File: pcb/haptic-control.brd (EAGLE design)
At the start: 40 x 160 mm, 117 parts, among them M1 SPH0641LM4H-1, P1 2P-PAD_1X3.5, P2 2P-PAD_1X3.5, P3 2P-PAD_1X3.5, P4 2P-PAD_1X3.5, U1 CC2642R, U10 FS8205, U11 MIC23159, U12 DRV2605L, U2 SST26VF064B, U3 ICM20948, U4 74LVC1G17, U5 DRV2605L, U6 PCA9306-DCU, U7 MTCH6301, U8 BQ51050B, U9 FS312F-G, X1 48MHz, X2 32.768kHz

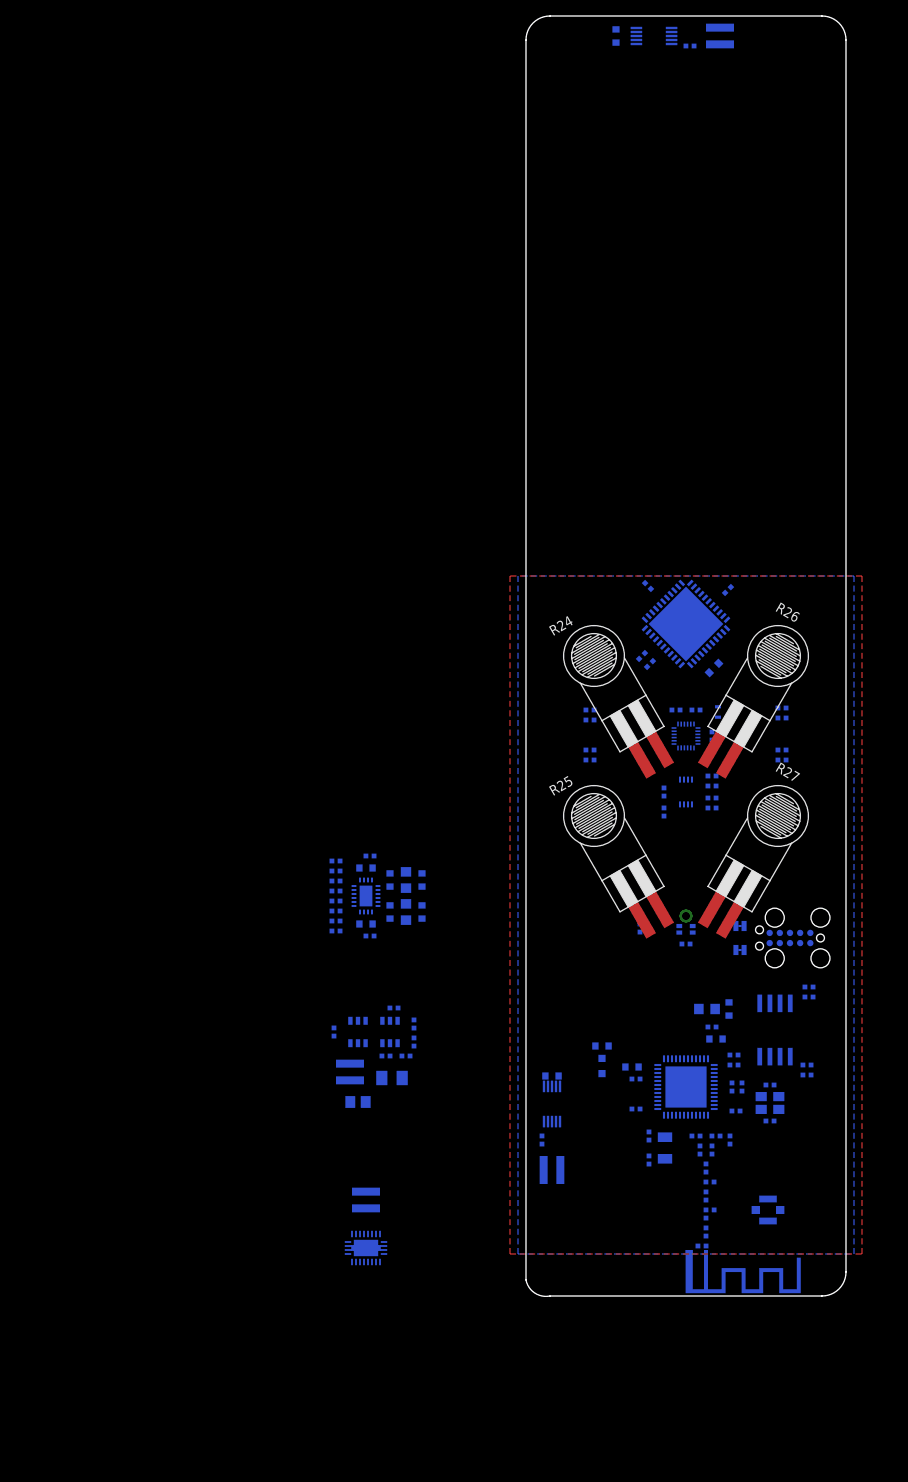
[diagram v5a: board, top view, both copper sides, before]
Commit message: Add QI and conect MCU
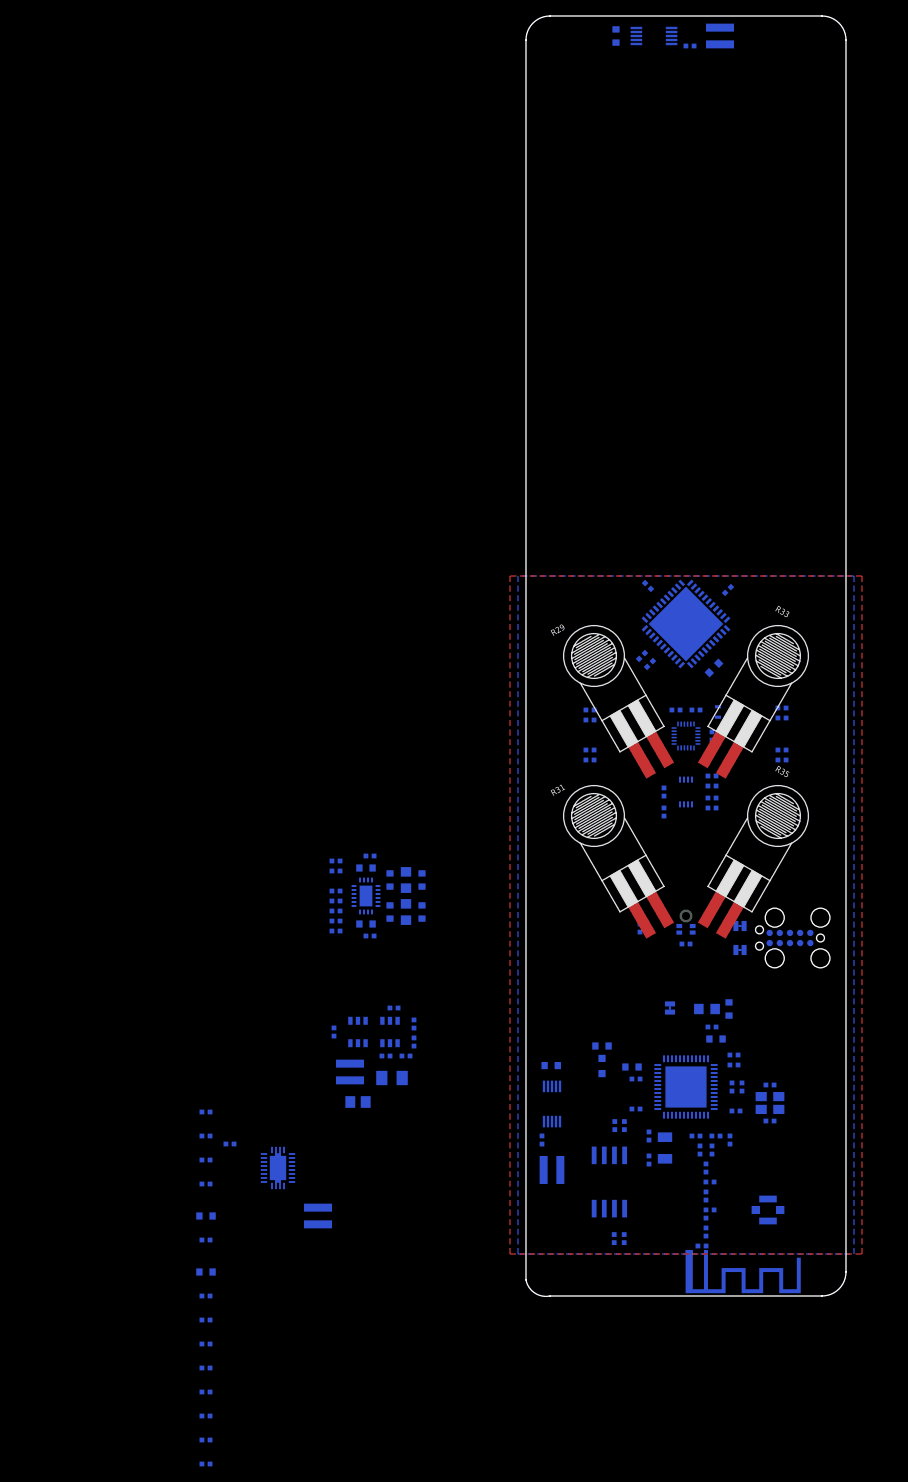
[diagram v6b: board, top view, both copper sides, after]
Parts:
- removed R1: 100k, Passive Components > Resistors > Chip Resistors:_0402
- added C52, C55, C56: 470p, Passive Components > Capacitors > Multilayer Ceramic Capacitors MLCC:_0402
- added C53, C57, C58, C59, C61: 100n, Passive Components > Capacitors > Multilayer Ceramic Capacitors MLCC:_0402
- added C54: 1u, Passive Components > Capacitors > Multilayer Ceramic Capacitors MLCC:0603_WAVE
- added C60: 10u, Passive Components > Capacitors > Multilayer Ceramic Capacitors MLCC:0603_WAVE
- added JP3: JUMPER-SMT_2_NC_TRACE_SILK, Utility > Board:SMT-JUMPER_2_NC_TRACE_SILK
- added R32, R34, R36: 3.4k, Passive Components > Resistors > Chip Resistors:_0402
- added R33, R35: FSR400-SHORT-TAIL, Interlink:FSR400-SHORT-TAIL
- added R37: 100k, Passive Components > Resistors > Chip Resistors:_0402
- C1: value 100n -> 1u; device Passive Components > Capacitors > Multilayer Ceramic Capacitors MLCC:_0402 -> Passive Components > Capacitors > Multilayer Ceramic Capacitors MLCC:0603_WAVE
- C10, C9: value 12p -> 22n
- C11, C12: value DNP -> 470n
- C13: value 1u -> 470p; device Passive Components > Capacitors > Multilayer Ceramic Capacitors MLCC:0603_WAVE -> Passive Components > Capacitors > Multilayer Ceramic Capacitors MLCC:_0402
- C14, C15, C19, C2: value 100n -> 4u7; device Passive Components > Capacitors > Multilayer Ceramic Capacitors MLCC:_0402 -> Passive Components > Capacitors > Multilayer Ceramic Capacitors MLCC:0603_WAVE
- C16, C39: value 4u7 -> 1u
- C18: value 100n -> 470p
- C21: value 100n -> 100u; device Passive Components > Capacitors > Multilayer Ceramic Capacitors MLCC:_0402 -> Passive Components > Capacitors > Multilayer Ceramic Capacitors MLCC:_1206
- C22, C44: value 100n -> DNP
- C23, C36: value 100n -> 22u; device Passive Components > Capacitors > Multilayer Ceramic Capacitors MLCC:_0402 -> Passive Components > Capacitors > Multilayer Ceramic Capacitors MLCC:0603_WAVE
- C24: value 10u -> 1p8; device Passive Components > Capacitors > Multilayer Ceramic Capacitors MLCC:0603_WAVE -> Passive Components > Capacitors > Multilayer Ceramic Capacitors MLCC:_0402
- C26: value 100n -> 12p; device Passive Components > Capacitors > Multilayer Ceramic Capacitors MLCC:_0402 -> Passive Components > Capacitors > Multilayer Ceramic Capacitors MLCC:_0402_SEL
- C27: value 22u -> 100n; device Passive Components > Capacitors > Multilayer Ceramic Capacitors MLCC:0603_WAVE -> Passive Components > Capacitors > Multilayer Ceramic Capacitors MLCC:_0402
- C28, C29: value 1p -> 100n
- C30: value 12p -> 1p
- C31: value 1p -> 22u; device Passive Components > Capacitors > Multilayer Ceramic Capacitors MLCC:_0402 -> Passive Components > Capacitors > Multilayer Ceramic Capacitors MLCC:0603_WAVE
- C32: value 1p8 -> 100n
- C33: value 12p -> 1p; device Passive Components > Capacitors > Multilayer Ceramic Capacitors MLCC:_0402_SEL -> Passive Components > Capacitors > Multilayer Ceramic Capacitors MLCC:_0402
- C34: value 470p -> 1p
- C35: value DNP -> 12p
- C37, C38, C46, C47: value 1u -> 100n; device Passive Components > Capacitors > Multilayer Ceramic Capacitors MLCC:0603_WAVE -> Passive Components > Capacitors > Multilayer Ceramic Capacitors MLCC:_0402
- C4: value 22u -> 4u7
- C40, C48, C49: value 470p -> 100n
- C41: value 470p -> DNP
- C42: value 4u7 -> 12p; device Passive Components > Capacitors > Multilayer Ceramic Capacitors MLCC:0603_WAVE -> Passive Components > Capacitors > Multilayer Ceramic Capacitors MLCC:_0402
- C43: value 100u -> 12p; device Passive Components > Capacitors > Multilayer Ceramic Capacitors MLCC:_1206 -> Passive Components > Capacitors > Multilayer Ceramic Capacitors MLCC:_0402
- C5: value 100n -> 1n
- C50: value 470p -> 1u; device Passive Components > Capacitors > Multilayer Ceramic Capacitors MLCC:_0402 -> Passive Components > Capacitors > Multilayer Ceramic Capacitors MLCC:0603_WAVE
- C6: value 22u -> 470p; device Passive Components > Capacitors > Multilayer Ceramic Capacitors MLCC:0603_WAVE -> Passive Components > Capacitors > Multilayer Ceramic Capacitors MLCC:_0402
- C7, C8: value 100n -> 10n
- L1: value 6u8 -> 1u
- L2: value BLM18HE152SN1 -> 1u; device Passive Components > Inductors, Chokes & Coils:_0603 -> Passive Components > Inductors, Chokes & Coils:_0805
- L3: value 2n4 -> BLM18HE152SN1; device Passive Components > Inductors, Chokes & Coils:_0402 -> Passive Components > Inductors, Chokes & Coils:_0603
- L4: value 2n4 -> 2N
- L6: value 2N -> 2n4
- L7: value 1u -> 2n4; device Passive Components > Inductors, Chokes & Coils:_0805 -> Passive Components > Inductors, Chokes & Coils:_0402
- L8: value 1u -> 6u8
- R11: value 10M -> 1k2
- R12: value 100 -> 140
- R14: value 49.9k -> 10k
- R15: value 1k -> 100k
- R16: value 100k -> 49.9k
- R17: value 100k -> 100
- R18: value 309k -> 1k
- R19: value 71.5k -> 10M
- R2: value 100k -> 309k
- R22: value 301k -> 4k7
- R23: value 158k -> 4k7
- R24, R25: value FSR400-SHORT-TAIL -> 100k; device Interlink:FSR400-SHORT-TAIL -> Passive Components > Resistors > Chip Resistors:_0402
- R26, R27: value FSR400-SHORT-TAIL -> 4k7; device Interlink:FSR400-SHORT-TAIL -> Passive Components > Resistors > Chip Resistors:_0402
- R28: value 3.4k -> 200k
- R29, R31: value 3.4k -> FSR400-SHORT-TAIL; device Passive Components > Resistors > Chip Resistors:_0402 -> Interlink:FSR400-SHORT-TAIL
- R3: value 4k7 -> 71.5k
- R6: value 4k7 -> 100k
- R7: value 200k -> 301k
- R8: value 4k7 -> 158k
- R9: value 4k7 -> 2k43
- U1: value CC2642R -> MIC23159; device Texas Instruments:QFN48 -> Microchip:VQFN20
- U10: value FS8205 -> DRV2605L; device Fortune:SOT23-6 -> Texas Instruments:VSSOP10
- U11: value MIC23159 -> DRV2605L; device Microchip:VQFN20 -> Texas Instruments:VSSOP10
- U12: value DRV2605L -> MTCH6301; device Texas Instruments:VSSOP10 -> Microchip:QFN44
- U2: value SST26VF064B -> BQ51050B; device Microchip:WSOIC8 -> Texas Instruments:VQFN20
- U3: value ICM20948 -> FS312F-G; device TDK:QFN20 -> Fortune:SOT23-6
- U4: value 74LVC1G17 -> FS8205; device Semiconductors > Integrated Circuits - ICs > Logic ICs > Logic Gates:SC70-5 -> Fortune:SOT23-6
- U5: value DRV2605L -> CC2642R; device Texas Instruments:VSSOP10 -> Texas Instruments:QFN48
- U6: value PCA9306-DCU -> SST26VF064B; device Texas Instruments:VSSOP8 -> Microchip:WSOIC8
- U7: value MTCH6301 -> 74LVC1G17; device Microchip:QFN44 -> Semiconductors > Integrated Circuits - ICs > Logic ICs > Logic Gates:SC70-5
- U8: value BQ51050B -> ICM20948; device Texas Instruments:VQFN20 -> TDK:QFN20
- U9: value FS312F-G -> PCA9306-DCU; device Fortune:SOT23-6 -> Texas Instruments:VSSOP8
- moved U11 113.4 mm to (16.0, 157.5), turned to 180 degrees
- moved C47 88.3 mm to (23.2, 70.0), turned to 270 degrees
- moved C19 86.3 mm to (-40.0, 10.0)
- moved C12 83.3 mm to (-40.0, -18.0)
- moved C45 83.0 mm to (21.2, 73.2)
- moved C11 82.5 mm to (-40.0, -21.0), turned to 0 degrees
- moved R9 81.2 mm to (-40.0, 14.0), turned to 0 degrees
- moved R10 79.8 mm to (-37.0, 19.0), turned to 0 degrees
- moved C26 78.0 mm to (22.5, 10.2), turned to 270 degrees
- moved U8 75.5 mm to (20.0, 70.0), turned to 180 degrees
- moved C7 74.3 mm to (-40.0, -6.00), turned to 0 degrees
- moved C8 73.6 mm to (-40.0, -9.00), turned to 0 degrees
- moved U12 73.6 mm to (20.0, 84.0), turned to 45 degrees
- moved C5 73.1 mm to (-40.0, -3.00), turned to 0 degrees
- moved R24 72.9 mm to (11.0, 7.17), flipped to the bottom, turned to 270 degrees
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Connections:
- removed net 3V3_PG: R17.1, U11.15
- new net !QI_CHG: R10.1, U2.7, U5.18
- new net N$39: R11.2, R12.2, R13.1, U2.14
- new net N$40: R11.1, U2.12
- new net N$41: C17.P$1, R13.2, U2.18
- new net N$42: R9.2, U2.10
- new net N$43: C11.1, U2.5
- new net N$44: C9.1, U2.6
- new net N$45: C7.1, U2.3
- new net N$46: C12.1, U2.16
- new net N$47: C10.1, U2.15
- new net N$48: C8.1, U2.17
- new net N$49: C10.2, C12.2, C5.2, C8.2, P1.2, U2.19
- new net N$50: C11.2, C3.1, C5.1, C7.2, C9.2, U2.2
- new net N$51: C3.2, P1.1
- new net N$53: JP3.2, U1.15
- new net QI_CTRL: R14.2, U2.13, U5.19
- net 1.8V: now also C14.P$1, C46.1, C47.1, L2.1, R26.2, R27.2, R7.1, U1.10, U8.13, U8.8, U9.2; no longer C18.1, C19.1, C42.P$1, L8.1, R22.1, R8.2, R9.2, U11.10, U3.13, U3.8, U6.2
- net 1V8_PG: now also R6.1, U1.12, U5.20; no longer R21.1, U11.12
- net 3.3V: now also C23.P$1, C4.P$1, C40.1, C57.1, C58.1, C59.1, C61.1, L1.1, L3.1, R22.2, R23.2, R24.2, R25.2, R28.2, R29.1, R31.1, R33.1, R35.1, R37.2, U1.17, U12.17, U12.28, U12.40, U6.8, U7.3; no longer C15.1, C22.1, C23.1, C25.1, C26.1, C27.P$1, C39.P$1, L2.1, L7.1, R17.2, R18.2, R24.1, R25.1, R26.1, R27.1, R3.2, R4.2, R5.2, R7.2, U11.17, U2.8, U4.3, U7.17, U7.28, U7.40
- net DBG_RX: now also U5.42
- net DBG_TX: now also U5.43
- net FLASH_CS: now also R21.1, U5.9, U6.1; no longer R2.1, U2.1
- net FLASH_MISO: now also U5.11, U6.2; no longer U2.2
- net FLASH_MOSI: now also U5.12, U6.5; no longer U2.5
- net FLASH_SCK: now also U5.10, U6.6; no longer U2.6
- net FSR_CH_N: now also C52.1, R31.2, R32.2, U5.38; no longer C49.1, R25.2, R29.2
- net FSR_CH_P: now also C51.1, R29.2, R30.2, U5.39; no longer C48.1, R24.2, R28.2
- net FSR_VOL_N: now also C56.1, R35.2, R36.2, U5.37; no longer C51.1, R27.2, R30.2
- net FSR_VOL_P: now also C55.1, R33.2, R34.2, U5.40; no longer C50.1, R26.2, R31.2
- net GBAT: now also C20.2, P2.2, R19.2, U3.6, U4.3; no longer C36.2, P1.2, R11.2, U10.3, U9.6
- net GND: now also C1.P$2, C13.2, C14.P$2, C15.P$2, C19.P$2, C2.P$2, C23.P$2, C27.2, C28.2, C29.2, C31.P$2, C32.2, C34.1, C36.P$2, C37.2, C38.2, C42.2, C46.2, C47.2, C50.P$2, C52.2, C53.2, C54.P$2, C55.2, C56.2, C57.2, C58.2, C59.2, C6.2, C60.P$2, C61.2, R12.1, R16.1, R18.1, R3.1, R32.1, R34.1, R36.1, R8.2, R9.1, U1.19, U1.2, U1.21, U1.5, U1.8, U10.4, U10.8, U11.4, U12.16, U12.29, U12.39, U12.45, U12.6, U2.1, U2.20, U2.25@0, U2.25@1, U2.25@2, U2.25@3, U2.25@4, U2.25@5, U2.25@6, U2.9, U4.1, U5.49, U6.4, U7.5, U8.18, U8.20, U8.9, U9.1; no longer C1.2, C10.2, C11.2, C12.2, C13.P$2, C14.2, C15.2, C19.2, C2.2, C20.2, C23.2, C24.P$2, C26.2, C27.P$2, C28.1, C3.2, C31.2, C34.2, C37.P$2, C38.P$2, C42.P$2, C46.P$2, C47.P$2, C5.2, C50.2, C6.P$2, C7.2, C8.2, C9.2, R11.1, R15.1, R23.2, R28.1, R29.1, R31.1, U1.49, U10.1, U11.19, U11.2, U11.21, U11.5, U12.4, U12.8, U2.4, U3.18, U3.20, U3.9, U4.5, U5.4, U5.8, U6.1, U7.16, U7.29, U7.39, U7.45, U7.6
- net I2S_CLK: now also U5.30
- net I2S_DATIN: now also U5.29
- net JTAG_TCKC: now also U5.25; no longer U1.25
- net JTAG_TDI: now also U5.27; no longer U1.27
- net JTAG_TDO: now also U5.26; no longer U1.26
- net JTAG_TMSC: now also U5.24; no longer U1.24
- net LRA_EN: now also U10.5, U11.5, U5.6; no longer U12.5, U5.5
- net MCU_!RESET: now also C25.1, JP3.1, R20.1, U5.35; no longer C14.1, R1.1, U1.35
- net MCU_SW: now also L8.1, U5.33; no longer L1.1, U1.33
- net MPU_INT: now also U5.28, U7.4; no longer U4.4
- net MPU_PWR: now also R5.1, U1.9, U5.21; no longer R20.1, U11.9
- net N$1: now also C34.2, L6.2, U5.2; no longer C28.2, L4.2, U1.2
- net N$10: now also C60.P$1, U12.7; no longer C24.P$1, U7.7
- net N$11: now also C48.1, R28.1, U9.7, U9.8; no longer C21.1, R7.1, U6.7, U6.8
- net N$12: now also C26.1, L4.1; no longer C33.1, L6.1
- net N$13: now also C24.1, C26.3; no longer C32.1, C33.3
- net N$14: now also C35.1, L7.1; no longer C30.1, L3.1
- net N$15: now also C33.1, L6.1; no longer C29.1, L4.1
- net N$16: now also C30.1, L4.2; no longer C31.1, L6.2
- net N$17: now also C22.1, C24.2; no longer C32.2, C35.1
- net N$18: now also C26.2; no longer C33.2
- net N$2: now also C39.P$1, U5.23; no longer C13.P$1, U1.23
- net N$21: now also U3.1, U4.4; no longer U10.4, U9.1
- net N$22: now also U3.3, U4.6; no longer U10.6, U9.3
- net N$23: now also C20.1, R17.1, U3.5; no longer C36.1, R12.1, U9.5
- net N$24: now also R18.2, U3.2; no longer R15.2, U9.2
- net N$25: now also R2.1, R3.2, U1.16; no longer R18.1, R19.2, U11.16
- net N$26: now also R4.1, U1.18; no longer R16.1, U11.18
- net N$27: now also U10.7; no longer U5.7
- net N$28: now also L1.2, U1.3; no longer L7.2, U11.3
- net N$29: now also C6.1, U1.14; no longer C40.1, U11.14
- net N$3: now also C33.2, L7.2, U5.1; no longer C29.2, L3.2, U1.1
- net N$30: now also L2.2, U1.4; no longer L8.2, U11.4
- net N$31: now also C13.1, U1.13; no longer C41.1, U11.13
- net N$32: now also R7.2, R8.1, U1.11; no longer R22.2, R23.1, U11.11
- net N$33: now also U10.9; no longer U5.9
- net N$34: now also U11.7; no longer U12.7
- net N$35: now also U11.9; no longer U12.9
- net N$36: now also C50.P$1, U10.1; no longer C46.P$1, U5.1
- net N$37: now also C54.P$1, U11.1; no longer C47.P$1, U12.1
- net N$38: now also P2.1; no longer P1.1
- net N$4: now also U7.2, U8.12; no longer U3.12, U4.2
- net N$5: now also R26.1, U8.23, U9.3; no longer R8.1, U3.23, U6.3
- net N$6: now also R27.1, U8.24, U9.4; no longer R9.1, U3.24, U6.4
- net N$7: now also R24.1, U6.3; no longer R4.1, U2.3
- net N$8: now also R25.1, U6.7; no longer R5.1, U2.7
- net N$9: now also C45.1, U8.10; no longer C20.1, U3.10
- net PCAP_RX0: now also U12.27; no longer U7.27
- net PCAP_RX1: now also U12.26; no longer U7.26
- net PCAP_RX10: now also U12.14; no longer U7.14
- net PCAP_RX11: now also U12.11; no longer U7.11
- net PCAP_RX12: now also U12.10; no longer U7.10
- net PCAP_RX2: now also U12.25; no longer U7.25
- net PCAP_RX3: now also U12.24; no longer U7.24
- net PCAP_RX4: now also U12.23; no longer U7.23
- net PCAP_RX5: now also U12.22; no longer U7.22
- net PCAP_RX6: now also U12.21; no longer U7.21
- net PCAP_RX7: now also U12.20; no longer U7.20
- net PCAP_RX8: now also U12.19; no longer U7.19
- net PCAP_RX9: now also U12.15; no longer U7.15
- net PCAP_TX0: now also U12.33; no longer U7.33
- net PCAP_TX1: now also U12.32; no longer U7.32
- net PCAP_TX10: now also U12.42; no longer U7.42
- net PCAP_TX11: now also U12.43; no longer U7.43
- net PCAP_TX12: now also U12.13; no longer U7.13
- net PCAP_TX13: now also U12.12; no longer U7.12
- net PCAP_TX14: now also U12.5; no longer U7.5
- net PCAP_TX15: now also U12.4; no longer U7.4
- net PCAP_TX16: now also U12.3; no longer U7.3
- net PCAP_TX17: now also U12.2; no longer U7.2
- net PCAP_TX2: now also U12.31; no longer U7.31
- net PCAP_TX3: now also U12.30; no longer U7.30
- net PCAP_TX4: now also U12.34; no longer U7.34
- net PCAP_TX5: now also U12.38; no longer U7.38
- net PCAP_TX6: now also U12.37; no longer U7.37
- net PCAP_TX7: now also U12.36; no longer U7.36
- net PCAP_TX8: now also U12.35; no longer U7.35
- net PCAP_TX9: now also U12.41; no longer U7.41
- net SCL: now also R22.1, R23.1, U10.2, U11.2, U12.44, U5.15, U9.6; no longer R3.1, R6.1, U12.2, U5.2, U6.6, U7.44
- net SDA: now also U10.3, U11.3, U12.1, U5.16, U9.5; no longer U12.3, U5.3, U6.5, U7.1
- net TC_!RESET: now also R37.1, U12.18, U5.31; no longer R10.1, U7.18
- net TC_INT: now also U12.8, U5.32; no longer U7.8
- net VBAT: now also C1.P$1, C15.P$1, C19.P$1, C2.P$1, C21.1, C49.1, C53.1, R15.2, R17.2, R4.2, R5.2, U1.1, U1.20, U1.6, U1.7, U10.10, U10.6, U11.10, U2.4; no longer C17.P$1, C37.P$1, C38.P$1, C43.1, C44.1, C45.1, R12.2, R13.2, R16.2, R20.2, U11.1, U11.20, U11.7, U12.10, U12.6, U5.10, U5.6
- net VBAT_SNS: now also C18.1, R15.1, R16.2, U5.36; no longer C34.1, R13.1, R14.2
- net VDDR: now also C36.P$1, C37.1, C38.1, L8.2, U5.45, U5.48; no longer C6.P$1, C7.1, C8.1, L1.2, U1.45, U1.48
- net VDDS: now also C27.1, C28.1, C29.1, C31.P$1, C32.1, L3.2, R20.2, U5.13, U5.22, U5.34, U5.44; no longer C1.1, C2.1, C3.1, C4.P$1, C5.1, L2.2, R1.2, U1.13, U1.22, U1.34, U1.44
- net XTAL_32K_Q1: now also C43.1, U5.3; no longer C10.1, U1.3
- net XTAL_32K_Q2: now also C42.1, U5.4; no longer C9.1, U1.4
- net XTAL_48M_N: now also C44.1, U5.46; no longer C12.1, U1.46
- net XTAL_48M_P: now also C41.1, U5.47; no longer C11.1, U1.47

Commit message: added notes to schematic
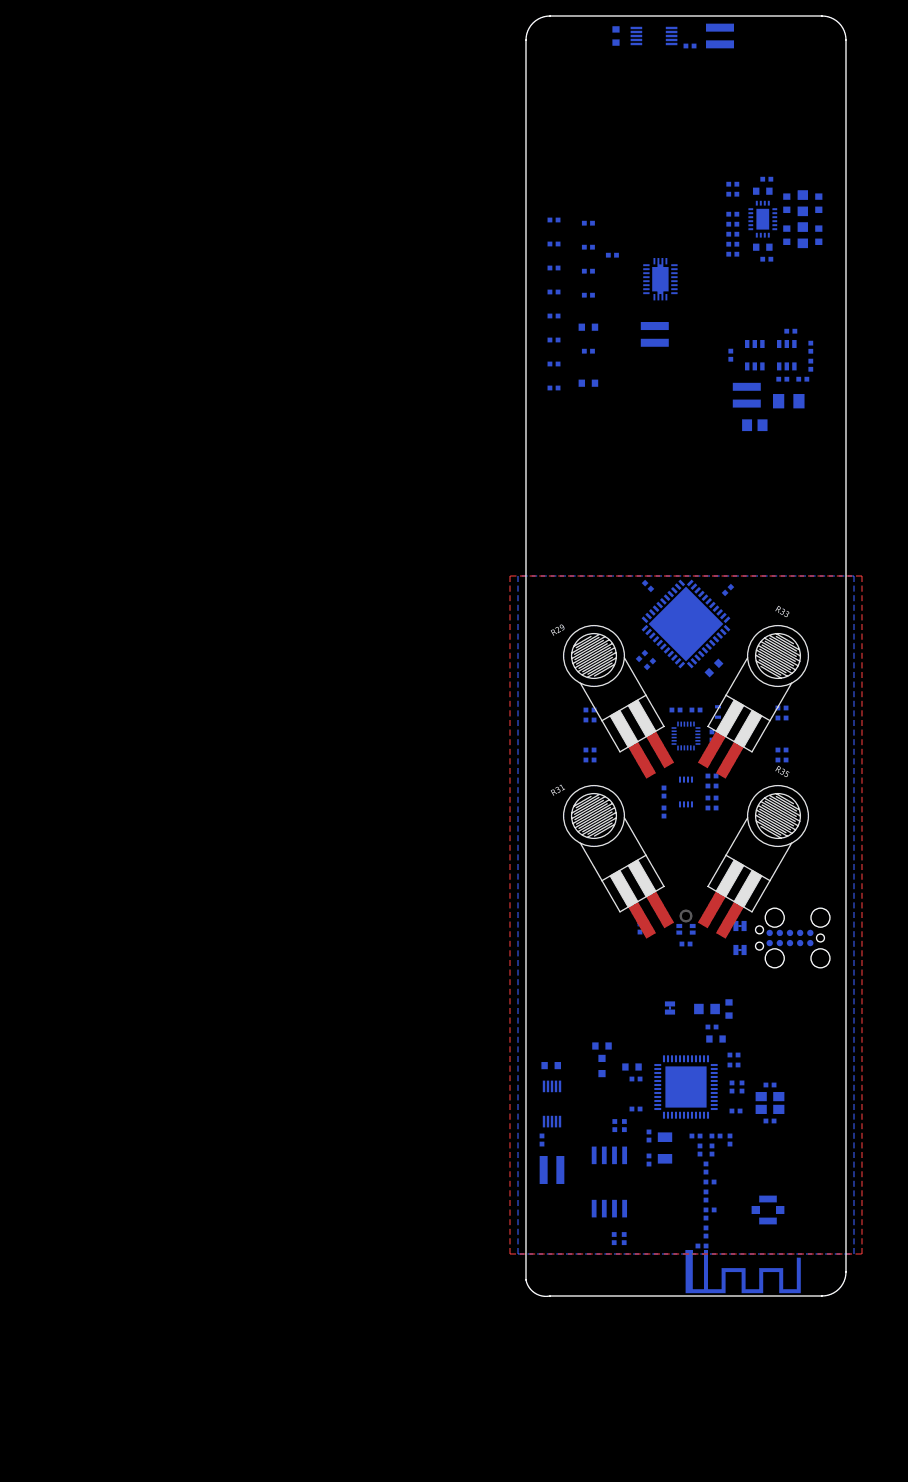
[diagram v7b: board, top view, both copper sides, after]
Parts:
- moved C10 141.4 mm to (3.50, 122.5)
- moved C11 141.4 mm to (3.50, 113.5)
- moved C12 141.4 mm to (3.50, 116.5)
- moved C3 141.4 mm to (3.50, 134.5)
- moved C5 141.4 mm to (3.50, 131.5)
- moved C7 141.4 mm to (3.50, 128.5)
- moved C8 141.4 mm to (3.50, 125.5)
- moved C9 141.4 mm to (3.50, 119.5)
- moved C17 120.9 mm to (7.80, 114.1)
- moved C19 120.9 mm to (7.80, 121.1)
- moved R10 120.9 mm to (10.8, 130.1)
- moved R11 120.9 mm to (7.80, 128.1)
- moved R12 120.9 mm to (7.80, 134.1)
- moved R13 120.9 mm to (7.80, 131.1)
- moved R14 120.9 mm to (7.80, 118.1)
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
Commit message: minor component placement and silkscreen changes
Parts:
- added U$3: (no value), Utility > Silkscreen:DESIGNEDINPT
- L1, L2, L8: device Passive Components > Inductors, Chokes & Coils:_0805 -> Passive Components > Inductors, Chokes & Coils:_0806
- moved R12 98.5 mm to (10.0, 35.6), turned to 270 degrees
- moved R13 95.5 mm to (8.80, 35.6), turned to 90 degrees
- moved C3 94.3 mm to (4.40, 40.2), turned to 270 degrees
- moved R11 92.6 mm to (12.4, 35.6), turned to 270 degrees
- moved C5 91.4 mm to (5.70, 40.1), turned to 270 degrees
- moved R4 90.5 mm to (32.8, 49.1), turned to 0 degrees
- moved R3 90.0 mm to (37.0, 49.7), turned to 0 degrees
- moved C8 89.8 mm to (6.00, 35.7), turned to 90 degrees
- moved C10 89.1 mm to (6.00, 33.4), turned to 90 degrees
- moved C2 87.6 mm to (33.3, 50.6), turned to 180 degrees
- moved R2 87.5 mm to (37.0, 51.0), turned to 180 degrees
- moved U2 87.4 mm to (10.0, 40.0), turned to 270 degrees
- moved R10 85.9 mm to (10.9, 44.2), turned to 90 degrees
- moved C4 85.2 mm to (26.1, 52.1), turned to 90 degrees
- moved L1 84.9 mm to (28.1, 52.0), turned to 90 degrees
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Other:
- board text added: "1920"
- board text added: "3V3"
- board text added: "4.2V Lipo"
- board text added: "DBG UART"
- board text added: "DRX"
- board text added: "DTX"
- board text added: "GND"
- board text added: "MIC"
- board text added: "Non TagConnect Compliant"
- board text added: "QI Coil"
- board text added: "RST"
- board text added: "TCK"
- board text added: "TDI"
- board text added: "TDO"
- board text added: "TMS"
